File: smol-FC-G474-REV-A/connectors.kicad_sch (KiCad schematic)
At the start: 49 parts, among them J2 ESC, J3 RX (ELRS), J4 GPS, J5 PWM/Action CAM, J6 CAM, J7 VTX, Q1 BC817

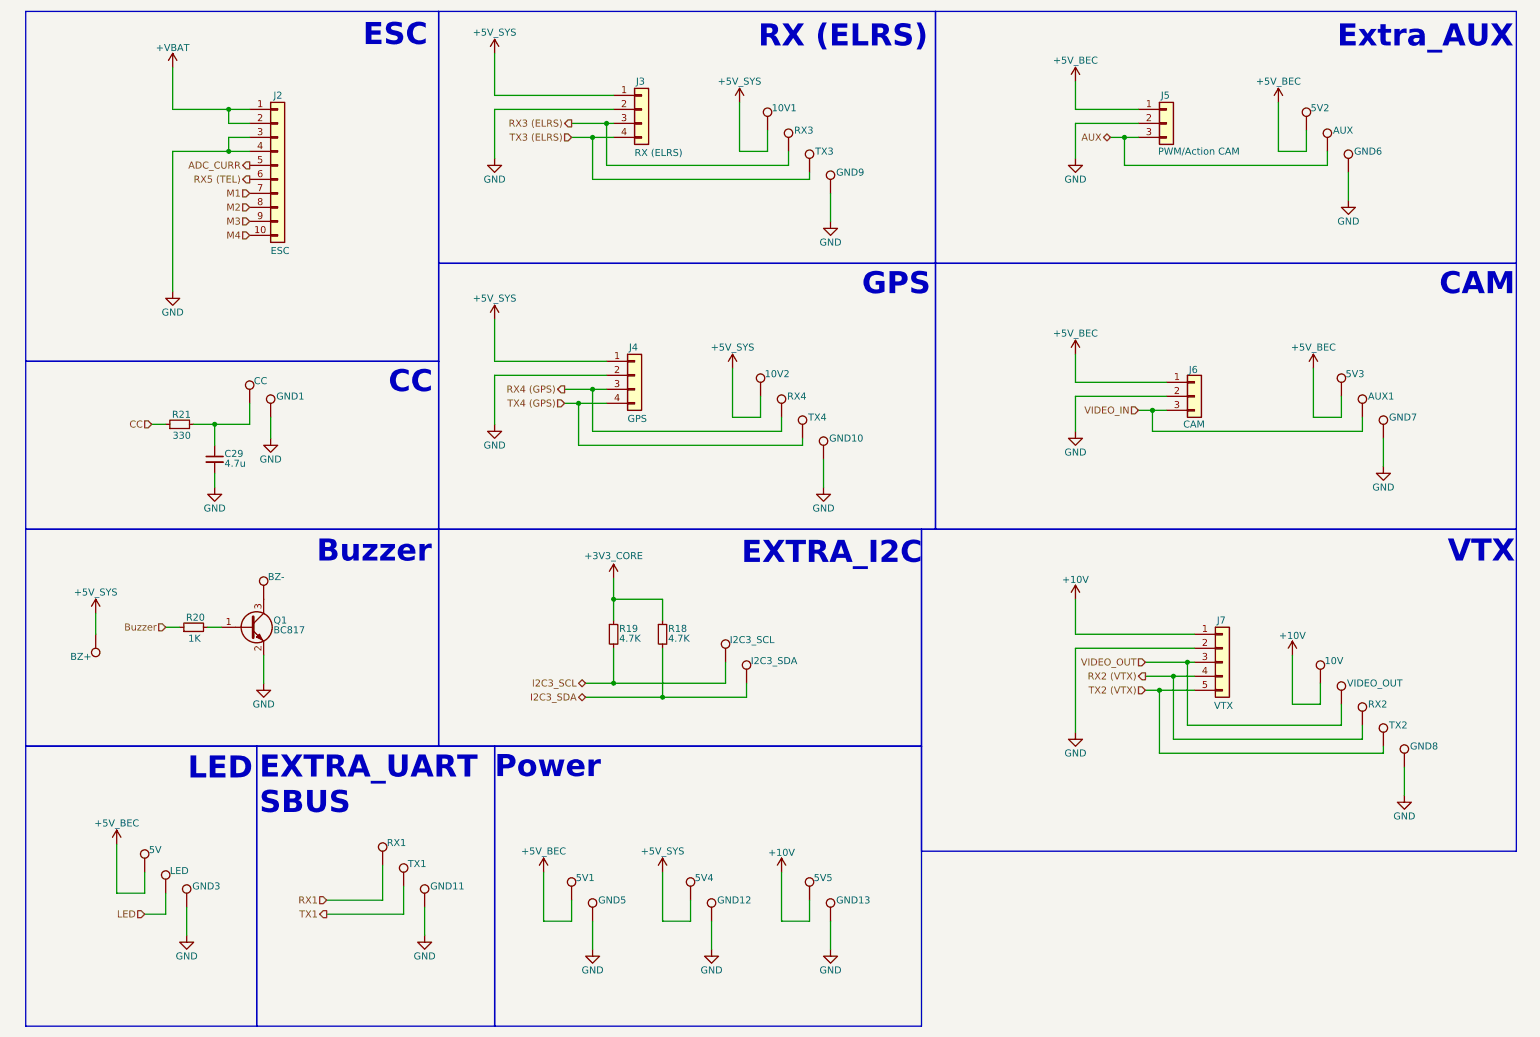
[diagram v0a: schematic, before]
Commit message: Updated Buck-5V doc, added Buck 5V/10V and LDO for 3v3 on schematic
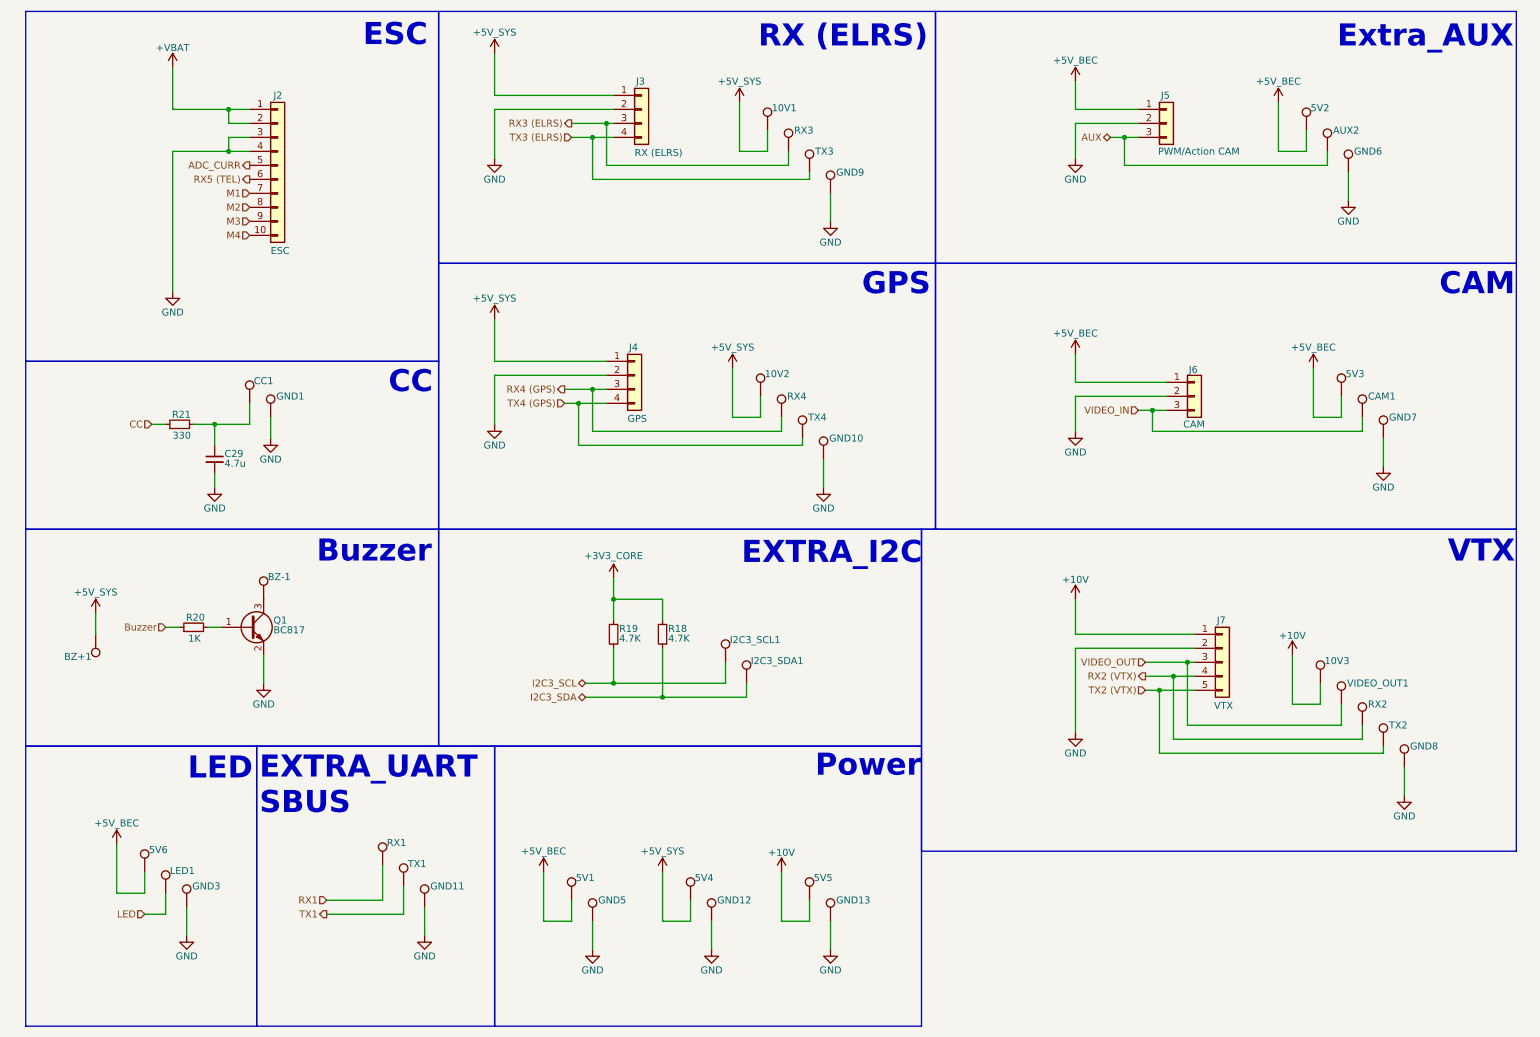
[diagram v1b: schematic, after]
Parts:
- renumbered 10V to 10V3, 5V to 5V6, AUX to AUX2, BZ+ to BZ+1, BZ- to BZ-1, AUX1 to CAM1, CC to CC1, I2C3_SCL to I2C3_SCL1, I2C3_SDA to I2C3_SDA1, LED to LED1, VIDEO_OUT to VIDEO_OUT1
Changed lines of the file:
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@@
 	(text "Power\n"
 		(exclude_from_sim no)
-		(at 107.442 149.86 0)
+		(at 165.608 149.606 0)
 		(effects
 			(font
@@
 		(in_pos_files yes)
 		(dnp no)
-		(property "Reference" "VIDEO_OUT"
+		(property "Reference" "VIDEO_OUT1"
 			(at 252.476 134.62 0)
 			(show_name no)
@@
 			(project "smol-FC-G474-REV-A"
 				(path "/650874a8-efa2-4da6-bfd2-a5dde0a9b2ac/2ae5d19c-c4f8-463c-a9e0-b776209965fe"
-					(reference "VIDEO_OUT")
+					(reference "VIDEO_OUT1")
 					(unit 1)
 				)
@@
 		(in_pos_files yes)
 		(dnp no)
-		(property "Reference" "10V"
+		(property "Reference" "10V3"
 			(at 248.412 130.556 0)
 			(show_name no)
@@
 			(project "smol-FC-G474-REV-A"
 				(path "/650874a8-efa2-4da6-bfd2-a5dde0a9b2ac/2ae5d19c-c4f8-463c-a9e0-b776209965fe"
-					(reference "10V")
+					(reference "10V3")
 					(unit 1)
 				)
@@
 		(in_pos_files yes)
 		(dnp no)
-		(property "Reference" "I2C3_SCL"
+		(property "Reference" "I2C3_SCL1"
 			(at 140.462 126.746 0)
 			(show_name no)
@@
 			(project "smol-FC-G474-REV-A"
 				(path "/650874a8-efa2-4da6-bfd2-a5dde0a9b2ac/2ae5d19c-c4f8-463c-a9e0-b776209965fe"
-					(reference "I2C3_SCL")
+					(reference "I2C3_SCL1")
 					(unit 1)
 				)
@@
 		(in_pos_files yes)
 		(dnp no)
-		(property "Reference" "AUX"
+		(property "Reference" "AUX2"
 			(at 249.936 34.29 0)
 			(show_name no)
@@
 			(project "smol-FC-G474-REV-A"
 				(path "/650874a8-efa2-4da6-bfd2-a5dde0a9b2ac/2ae5d19c-c4f8-463c-a9e0-b776209965fe"
-					(reference "AUX")
+					(reference "AUX2")
 					(unit 1)
 				)
@@
 		(in_pos_files yes)
 		(dnp no)
-		(property "Reference" "AUX1"
+		(property "Reference" "CAM1"
 			(at 256.286 82.55 0)
 			(show_name no)
@@
 			(project "smol-FC-G474-REV-A"
 				(path "/650874a8-efa2-4da6-bfd2-a5dde0a9b2ac/2ae5d19c-c4f8-463c-a9e0-b776209965fe"
-					(reference "AUX1")
+					(reference "CAM1")
 					(unit 1)
 				)
@@
 		(in_pos_files yes)
 		(dnp no)
-		(property "Reference" "I2C3_SDA"
+		(property "Reference" "I2C3_SDA1"
 			(at 144.272 130.556 0)
 			(show_name no)
@@
 			(project "smol-FC-G474-REV-A"
 				(path "/650874a8-efa2-4da6-bfd2-a5dde0a9b2ac/2ae5d19c-c4f8-463c-a9e0-b776209965fe"
-					(reference "I2C3_SDA")
+					(reference "I2C3_SDA1")
 					(unit 1)
 				)
@@
 		(in_pos_files yes)
 		(dnp no)
-		(property "Reference" "5V"
+		(property "Reference" "5V6"
 			(at 35.052 164.846 0)
 			(show_name no)
@@
 			(project "smol-FC-G474-REV-A"
 				(path "/650874a8-efa2-4da6-bfd2-a5dde0a9b2ac/2ae5d19c-c4f8-463c-a9e0-b776209965fe"
-					(reference "5V")
+					(reference "5V6")
 					(unit 1)
 				)
@@
 		(in_pos_files yes)
 		(dnp no)
-		(property "Reference" "LED"
+		(property "Reference" "LED1"
 			(at 38.862 168.656 0)
 			(show_name no)
@@
 			(project "smol-FC-G474-REV-A"
 				(path "/650874a8-efa2-4da6-bfd2-a5dde0a9b2ac/2ae5d19c-c4f8-463c-a9e0-b776209965fe"
-					(reference "LED")
+					(reference "LED1")
 					(unit 1)
 				)
@@
 		(in_pos_files yes)
 		(dnp no)
-		(property "Reference" "BZ-"
+		(property "Reference" "BZ-1"
 			(at 56.642 115.316 0)
 			(show_name no)
@@
 			(project "smol-FC-G474-REV-A"
 				(path "/650874a8-efa2-4da6-bfd2-a5dde0a9b2ac/2ae5d19c-c4f8-463c-a9e0-b776209965fe"
-					(reference "BZ-")
+					(reference "BZ-1")
 					(unit 1)
 				)
@@
 		(in_pos_files yes)
 		(dnp no)
-		(property "Reference" "BZ+"
+		(property "Reference" "BZ+1"
 			(at 24.638 129.794 0)
 			(show_name no)
@@
 			(project "smol-FC-G474-REV-A"
 				(path "/650874a8-efa2-4da6-bfd2-a5dde0a9b2ac/2ae5d19c-c4f8-463c-a9e0-b776209965fe"
-					(reference "BZ+")
+					(reference "BZ+1")
 					(unit 1)
 				)
@@
 		(in_pos_files yes)
 		(dnp no)
-		(property "Reference" "CC"
+		(property "Reference" "CC1"
 			(at 54.102 79.756 0)
 			(show_name no)
@@
 			(project "smol-FC-G474-REV-A"
 				(path "/650874a8-efa2-4da6-bfd2-a5dde0a9b2ac/2ae5d19c-c4f8-463c-a9e0-b776209965fe"
-					(reference "CC")
+					(reference "CC1")
 					(unit 1)
 				)

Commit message: Changed 10V buck to 9V buck
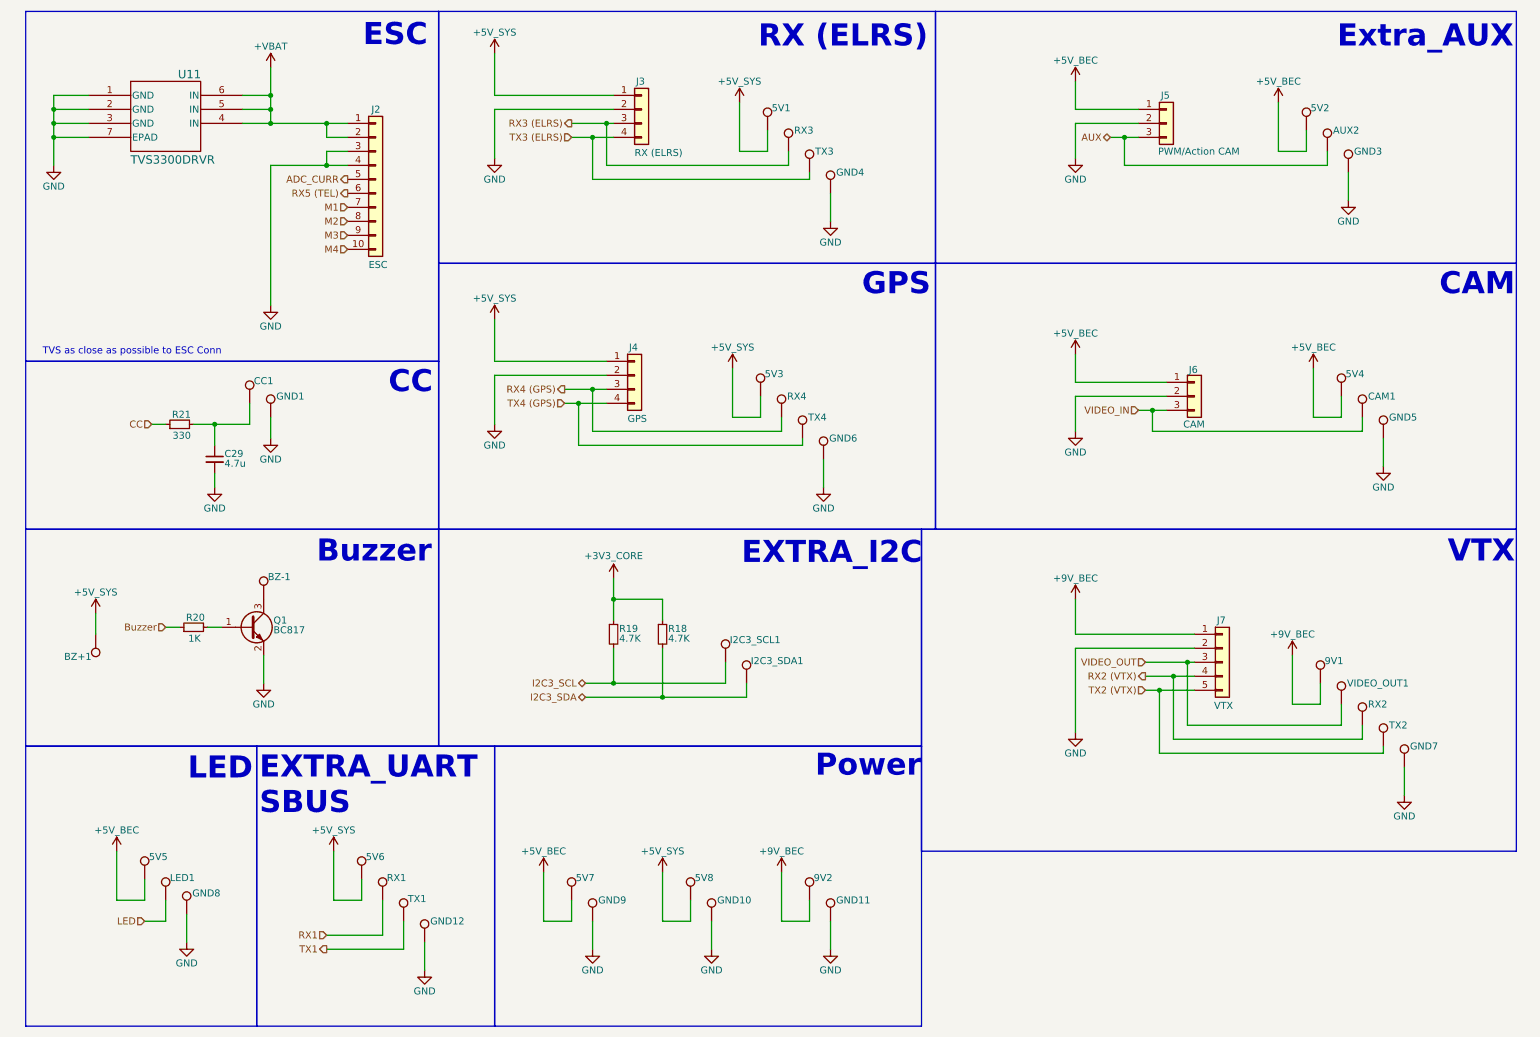
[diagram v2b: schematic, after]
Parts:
- added 5V6: TestPoint, symbol Connector:TestPoint
- added U11: TVS3300DRVR, symbol TVS3300DRVR:TVS3300DRVR
- Q1: footprint Package_TO_SOT_SMD:SOT-23 -> (none)
- renumbered 10V1 to 5V1, 10V2 to 5V3, 5V3 to 5V4, 5V6 to 5V5, 5V1 to 5V7, 5V4 to 5V8, 10V3 to 9V1, 5V5 to 9V2, GND12 to GND10, GND13 to GND11, GND11 to GND12, GND6 to GND3, GND9 to GND4, GND7 to GND5, GND10 to GND6, GND8 to GND7, GND3 to GND8, GND5 to GND9
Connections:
- net +5V_SYS: now also 5V6.1
- net +VBAT: now also U11.4 (IN), U11.5 (IN), U11.6 (IN)
- net GND: now also U11.1 (GND), U11.2 (GND), U11.3 (GND), U11.7 (EPAD)
- net +10V renamed +9V_BEC
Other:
- note added: "TVS as close as possible to ESC Conn"
- moved on the sheet: 5V5, GND12, GND8, J2, LED1, RX1, TX1

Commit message: Attached footprints and finalized schematic.
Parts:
- 5V1, 5V2, 5V3, 5V4, 5V5, 5V6, 5V7, 5V8, 9V1, 9V2, AUX2, BZ+1, BZ-1, CAM1, CC1, GND1, GND10, GND11, GND12, GND3, GND4, GND5, GND6, GND7, GND8, GND9, I2C3_SCL1, I2C3_SDA1, LED1, RX1, RX2, RX3, RX4, TX1, TX2, TX3, TX4, VIDEO_OUT1: footprint (none) -> pad-2.2x1.6:pad-2.2x1.6; now left out of the parts list
- C29: footprint (none) -> Capacitor_SMD:C_0402_1005Metric
- J2: footprint (none) -> Connector_JST:JST_SH_SM10B-SRSS-TB_1x10-1MP_P1.00mm_Horizontal
- J3, J4: footprint (none) -> Connector_JST:JST_SH_SM04B-SRSS-TB_1x04-1MP_P1.00mm_Horizontal
- J5, J6: footprint (none) -> Connector_JST:JST_SH_SM03B-SRSS-TB_1x03-1MP_P1.00mm_Horizontal
- J7: footprint (none) -> Connector_JST:JST_SH_SM05B-SRSS-TB_1x05-1MP_P1.00mm_Horizontal
- Q1: footprint (none) -> Package_TO_SOT_SMD:SOT-23
- R18, R19, R20, R21: footprint (none) -> Resistor_SMD:R_0402_1005Metric
- U11: footprint (none) -> TVS3300DRVR:DRV6_1X1P6_TEX
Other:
- title: smol-FC-G474 -> smol-FC-G474-REV-A

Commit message: Finalized schematic, added power mux
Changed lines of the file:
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@@
 		(comment 1 "License: CERN-OHL-W v2")
 		(comment 2 "GitHub: https://github.com/Def12345678/smol-FC-G474-REV-A")
-		(comment 3 "BEC 5A/3A, 10V/3A | Baro, OSD Chip and 16MB blackbox")
+		(comment 3 "BEC 5A/3A, 9V/3A | Baro, OSD Chip and 16MB blackbox")
 		(comment 4 "Open source flight controller on STM32G4, 20x20 3.5mm hole")
 	)

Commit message: In progress PCB layout
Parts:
- removed 5V6, 9V2, GND12, GND9: TestPoint, pad-2.2x1.6:pad-2.2x1.6, symbol Connector:TestPoint
- removed J3: RX (ELRS), Connector_JST:JST_SH_SM04B-SRSS-TB_1x04-1MP_P1.00mm_Horizontal, symbol Connector_Generic:Conn_01x04
- removed J4: GPS, Connector_JST:JST_SH_SM04B-SRSS-TB_1x04-1MP_P1.00mm_Horizontal, symbol Connector_Generic:Conn_01x04
- removed J5: PWM/Action CAM, Connector_JST:JST_SH_SM03B-SRSS-TB_1x03-1MP_P1.00mm_Horizontal, symbol Connector_Generic:Conn_01x03
- removed J6: CAM, Connector_JST:JST_SH_SM03B-SRSS-TB_1x03-1MP_P1.00mm_Horizontal, symbol Connector_Generic:Conn_01x03
- removed J7: VTX, Connector_JST:JST_SH_SM05B-SRSS-TB_1x05-1MP_P1.00mm_Horizontal, symbol Connector_Generic:Conn_01x05
- removed Q1: BC817, Package_TO_SOT_SMD:SOT-23, symbol Transistor_BJT:BC817
- added CURR1, GND4, M1, M2, M3, M4, TEL1, VBAT1: TestPoint, pad-2.2x1.6:pad-1.2x1.5, symbol Connector:TestPoint
- added Q1: BC817W, Package_TO_SOT_SMD:SOT-323_SC-70, symbol Transistor_BJT:BC817W
- 5V1: renamed from 5V2; footprint pad-2.2x1.6:pad-2.2x1.6 -> pad-2.2x1.6:pad-1.2x1.5
- 5V2: renamed from 5V1; footprint pad-2.2x1.6:pad-2.2x1.6 -> pad-2.2x1.6:pad-1.2x1.5
- 5V3, 5V4, 5V5, 9V1, BZ+1, BZ-1, CAM1, CC1, GND10, GND11, GND7, I2C3_SCL1, I2C3_SDA1, LED1, RX1, RX2, RX4, TX1, TX2, TX4, VIDEO_OUT1: footprint pad-2.2x1.6:pad-2.2x1.6 -> pad-2.2x1.6:pad-1.2x1.5
- 5V6: renamed from 5V7; footprint pad-2.2x1.6:pad-2.2x1.6 -> pad-2.2x1.6:pad-1.2x1.5
- 5V7: renamed from 5V8; footprint pad-2.2x1.6:pad-2.2x1.6 -> pad-2.2x1.6:pad-1.2x1.5
- AUX1: renamed from AUX2; footprint pad-2.2x1.6:pad-2.2x1.6 -> pad-2.2x1.6:pad-1.2x1.5
- GND2: renamed from GND3; footprint pad-2.2x1.6:pad-2.2x1.6 -> pad-2.2x1.6:pad-1.2x1.5
- GND3: renamed from GND4; footprint pad-2.2x1.6:pad-2.2x1.6 -> pad-2.2x1.6:pad-1.2x1.5
- GND5: renamed from GND6; footprint pad-2.2x1.6:pad-2.2x1.6 -> pad-2.2x1.6:pad-1.2x1.5
- GND6: renamed from GND5; footprint pad-2.2x1.6:pad-2.2x1.6 -> pad-2.2x1.6:pad-1.2x1.5
- GND8: renamed from GND1; footprint pad-2.2x1.6:pad-2.2x1.6 -> pad-2.2x1.6:pad-1.2x1.5
- GND9: renamed from GND8; footprint pad-2.2x1.6:pad-2.2x1.6 -> pad-2.2x1.6:pad-1.2x1.5
- R17: renamed from R19; value 4.7K -> 4.7k
- R18: value 4.7K -> 4.7k
- R19: renamed from R20; value 1K -> 1k
- RX3: renamed from TX3; footprint pad-2.2x1.6:pad-2.2x1.6 -> pad-2.2x1.6:pad-1.2x1.5
- TX3: renamed from RX3; footprint pad-2.2x1.6:pad-2.2x1.6 -> pad-2.2x1.6:pad-1.2x1.5
- renumbered C29 to C28, J2 to J1, R21 to R16, U11 to U7
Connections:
- net +VBAT: now also VBAT1.1
- net ADC_CURR: now also CURR1.1
- net CC: now also C28.1, CC1.1, R16.2
- net GND: now also GND4.1, Q1.2 (E)
- net M1: now also M1.1
- net M2: now also M2.1
- net M3: now also M3.1
- net M4: now also M4.1
- net RX3 (ELRS): now also RX3.1; no longer TX3.1
- net RX5 (TEL): now also TEL1.1
- net TX3 (ELRS): now also TX3.1; no longer RX3.1
- net BZ_G: now reaches R19.2
- net BZ_G: now also Q1.1 (B)
- net BZ-: now reaches BZ-1.1
- net BZ-: now also Q1.3 (C)
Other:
- moved on the sheet: 5V1, 5V2, 5V3, 5V4, 5V6, 5V7, 9V1, AUX1, BZ+1, BZ-1, C28, CAM1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

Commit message: changed size of cap on buck's
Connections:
- net CC: no longer C28.1, CC1.1, R16.2
- new net CC_P: C28.1, CC1.1, R16.2
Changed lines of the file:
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@@
 		)
 	)
-	(label "CC"
+	(label "CC_P"
 		(at 95.25 123.19 0)
 		(effects
@@
 	)
 	(hierarchical_label "TX1"
-		(shape output)
+		(shape input)
 		(at 66.04 181.61 180)
 		(effects
@@
 	)
 	(hierarchical_label "VIDEO_IN"
-		(shape input)
+		(shape output)
 		(at 242.57 85.09 180)
 		(effects
@@
 	)
 	(hierarchical_label "RX1"
-		(shape input)
+		(shape output)
 		(at 66.04 179.07 180)
 		(effects
